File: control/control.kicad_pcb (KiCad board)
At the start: 2 copper layers, 39.1 x 45.8 mm, 37 parts, among them J1 AVR-ISP-6, J2 Conn_01x07_Pin, J3 Conn_01x02_Pin, J4 Conn_01x04_Socket, P1 Conn_01x03_Pin, P2 Conn_01x03_Pin, P3 Conn_01x03_Pin, P4 Conn_01x03_Pin, SW1 SW_Push, U2 ATmega328P-A, Y1 16MHz

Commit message: Revised hardware
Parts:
- removed HOLE1, HOLE2: MountingHole_3.2mm_M3, MountingHole:MountingHole_3.2mm_M3
- removed LED1: LED1, LED_THT:LED_D4.0mm
- removed SW1: SW_Push, Button_Switch_SMD:SW_SPST_SKQG_WithoutStem
- added C12: 0.1uF, Capacitor_SMD:C_0805_2012Metric, F.Cu at (135.7, 84.4)
- added C14: 22uF, Capacitor_SMD:C_0805_2012Metric, F.Cu at (141.7, 90.8)
- added C15: 22uF, Capacitor_SMD:C_0805_2012Metric, F.Cu at (143.8, 90.8)
- added C16: 22uF, Capacitor_SMD:C_0805_2012Metric, F.Cu at (145.9, 90.8)
- added C17: 0.1uF, Capacitor_SMD:C_0805_2012Metric, F.Cu at (150.1, 87.3)
- added I2C1: FS2, Connector_JST:JST_XH_B4B-XH-A_1x04_P2.50mm_Vertical, F.Cu at (126.4, 60.6)
- added I2C2: FS1, Connector_JST:JST_XH_B4B-XH-A_1x04_P2.50mm_Vertical, F.Cu at (161.1, 60.6)
- added ISC3: MAIN, Connector_JST:JST_XH_B5B-XH-A_1x05_P2.50mm_Vertical, F.Cu at (156.2, 98.1)
- added JP1: Jumper_3_Open, Jumper:SolderJumper-3_P2.0mm_Open_TrianglePad1.0x1.5mm, F.Cu at (151.7, 80.2)
- added L2: 3.3uH, Inductor_SMD:L_Taiyo-Yuden_NR-60xx, F.Cu at (130.6, 85.4)
- added LED9: LED1, LED_THT:LED_D4.0mm, F.Cu at (131.4, 74.1)
- added R6: 33.2k, Resistor_SMD:R_0603_1608Metric, F.Cu at (152.5, 91.0)
- added R7: 10k, Resistor_SMD:R_0603_1608Metric, F.Cu at (138.9, 87.8)
- added R8: 10k, Resistor_SMD:R_0603_1608Metric, F.Cu at (138.6, 90.9)
- added R9: 54.9k, Resistor_SMD:R_0603_1608Metric, F.Cu at (125.8, 91.8)
- added REF**: MountingHole_3.2mm_M3, MountingHole:MountingHole_3.2mm_M3, F.Cu at (119.3, 95.3)
- added REF**: MountingHole_3.2mm_M3, MountingHole:MountingHole_3.2mm_M3, F.Cu at (131.3, 67.8)
- added S5: Conn_01x03_Pin, Connector_JST:JST_EH_B3B-EH-A_1x03_P2.50mm_Vertical, F.Cu at (124.0, 88.5)
- added SW2: SW_Push, Button_Switch_SMD:SW_SPST_B3U-1000P-B, F.Cu at (152.1, 74.7)
- added U3: ~, Package_TO_SOT_SMD:TSOT-23-6, F.Cu at (146.9, 87.3)
- C1, C2, C3, C4: value 22uF -> 100n; footprint Capacitor_SMD:C_0805_2012Metric -> Capacitor_SMD:C_0603_1608Metric
- C10, C9: value 100nF -> 22uF
- C11: value 10nF -> 22uF
- C6, C7: value 0.1uF -> 22uF
- C8: value 1uF -> 22uF
- J1: value AVR-ISP-6 -> Conn_01x02_Pin; footprint Connector_PinHeader_2.54mm:PinHeader_2x03_P2.54mm_Vertical_SMD -> Connector_JST:JST_XH_B2B-XH-A_1x02_P2.50mm_Vertical
- J2: value Conn_01x07_Pin -> Conn_01x04_Male; footprint Connector_JST:JST_XH_B7B-XH-A_1x07_P2.50mm_Vertical -> Connector_PinHeader_2.54mm:PinHeader_1x04_P2.54mm_Horizontal
- J4: value Conn_01x04_Socket -> Conn_01x07_Pin; footprint Connector_JST:JST_XH_B4B-XH-A_1x04_P2.50mm_Vertical -> Connector_JST:JST_XH_B7B-XH-A_1x07_P2.50mm_Vertical
- R2: value 420 -> 10k
- R5: value 54.9k -> 420
- U1: value ~ -> STM32F103C8Tx; footprint Package_TO_SOT_SMD:TSOT-23-6 -> Package_QFP:LQFP-48_7x7mm_P0.5mm
- U2: value ATmega328P-A -> ~; footprint Package_QFP:TQFP-32_7x7mm_P0.8mm -> Package_TO_SOT_SMD:TSOT-23-6
- Y1: value 16MHz -> 8Mhz
- moved J4 45.3 mm to (147.5, 60.6), turned to 180 degrees
- moved J2 37.9 mm to (162.0, 87.2), turned to 0 degrees
- moved J3 37.6 mm to (125.9, 95.5), turned to 0 degrees
- moved P1 34.6 mm to (162.7, 66.8), turned to 180 degrees
- moved J1 31.2 mm to (147.8, 95.5), turned to 0 degrees
- moved S1 28.4 mm to (124.0, 66.3), turned to 180 degrees
- moved Y1 25.8 mm to (147.4, 73.2)
- moved S4 24.6 mm to (124.0, 82.8), turned to 180 degrees
- moved P4 23.0 mm to (162.7, 83.0), turned to 180 degrees
- moved P2 20.7 mm to (162.7, 72.0), turned to 180 degrees
- moved U1 20.0 mm to (140.9, 73.6), turned to 180 degrees
- moved R5 19.6 mm to (128.1, 80.2), turned to -90 degrees
- moved C3 17.9 mm to (133.1, 80.3)
- moved C5 17.9 mm to (141.7, 87.3)
- moved C4 17.5 mm to (134.7, 80.3), turned to -90 degrees
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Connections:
- C1 pad 2: +5V -> +3.3V
- C10 pad 1: +5V -> +BATT
- C11 pad 1: +5V -> +BATT
- C2 pad 2: +5V -> +3.3V
- C3 pad 1: +BATT -> GND
- C3 pad 2: GND -> +3.3V
- C4 pad 1: +BATT -> +3.3V
- C5 pad 1: +BATT -> GND
- C5 pad 2: GND -> +3.3V
- C6 pad 1: Net-(U1-SW) -> GND
- C6 pad 2: Net-(U1-VBST) -> +3.3V
- C7 pad 1: Net-(U1-VFB) -> GND
- C8 pad 1: +5V -> GND
- C8 pad 2: GND -> +5V
- C9 pad 1: +5V -> +BATT
- J1 pad 1: MISO -> GND
- J1 pad 2: +5V -> +3.3V
- J2 pad 1: +5V -> +3.3V
- J2 pad 2: LED_{FIELD1} -> SWCLK
- J2 pad 3: LED_{FIELD2} -> SWDIO
- J2 pad 4: LED_{FIELD3} -> GND
- J4 pad 1: GND -> +5V
- J4 pad 2: +5V -> LED_{FIELD1}
- J4 pad 3: SDA -> LED_{FIELD2}
- J4 pad 4: SCL -> LED_{FIELD3}
- L1 pad 1: +5V -> +3.3V
- L1 pad 2: Net-(U1-SW) -> Net-(U3-SW)
- P1 pad 1: +5V -> +3.3V
- P2 pad 1: +5V -> +3.3V
- P3 pad 1: +5V -> +3.3V
- P4 pad 1: +5V -> +3.3V
- R1 pad 1: RESET -> GND
- R1 pad 2: +5V -> Net-(JP1-C)
- R2 pad 1: Net-(LED1-A) -> +3.3V
- R2 pad 2: +5V -> Net-(U1-NRST)
- R3 pad 2: Net-(U1-VFB) -> Net-(U3-VFB)
- R4 pad 1: Net-(U1-EN) -> Net-(U3-EN)
- R5 pad 1: +5V -> Net-(LED9-A)
- R5 pad 2: Net-(U1-VFB) -> +5V
- U1 pad 1: GND -> unconnected-(U1-VBAT-Pad1)
- U1 pad 2: Net-(U1-SW) -> unconnected-(U1-PC13-Pad2)
- U1 pad 3: +BATT -> unconnected-(U1-PC14-Pad3)
- U1 pad 4: Net-(U1-VFB) -> unconnected-(U1-PC15-Pad4)
- U1 pad 5: Net-(U1-EN) -> Net-(U1-PD0)
- U1 pad 6: Net-(U1-VBST) -> Net-(U1-PD1)
- U2 pad 1: LED_{FIELD4} -> GND
- U2 pad 2: unconnected-(U2-PD4-Pad2) -> Net-(U2-SW)
- U2 pad 3: GND -> +BATT
- U2 pad 4: +5V -> Net-(U2-VFB)
- U2 pad 5: GND -> Net-(U2-EN)
- U2 pad 6: +5V -> Net-(U2-VBST)
- Y1 pad 1: Net-(U2-XTAL2/PB7) -> Net-(U1-PD0)
- Y1 pad 3: Net-(U2-XTAL1/PB6) -> Net-(U1-PD1)
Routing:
- net +3.3V: track 0.00 -> 135.6 mm, vias 0 -> 3
- net SCL_{TOCTRL}: track 0.00 -> 55.9 mm
- net SDA_{TOCTRL}: track 0.00 -> 43.3 mm, vias 0 -> 2
- net SDA_{TOMAIN}: track 0.00 -> 41.0 mm, vias 0 -> 1
- net +5V: track 82.1 -> 45.2 mm, vias 11 -> 8
- net SWDIO: track 0.00 -> 33.4 mm, vias 0 -> 1
- net SWCLK: track 0.00 -> 32.2 mm, vias 0 -> 1
- net SER5: track 0.00 -> 27.4 mm, vias 0 -> 2
- net RESET: track 26.8 -> 0.00 mm, vias 4 -> 0
- net SCL_{TOMAIN}: track 0.00 -> 23.7 mm, vias 0 -> 1
- net BUZ: track 34.1 -> 11.6 mm, vias 2 -> 0
- net SCK: track 21.2 -> 0.00 mm, vias 2 -> 0
- net SDA: track 20.4 -> 0.00 mm, vias 1 -> 0
- net SCL: track 20.3 -> 0.00 mm, vias 1 -> 0
- net MISO: track 19.8 -> 0.00 mm, vias 2 -> 0
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- added copper zone on F.Cu, net +3.3V
- added copper zone on F.Cu, net +BATT
- added copper zone on B.Cu, net GND
- removed copper zone on F.Cu, net +5V
- removed copper zone on B.Cu, net +BATT
- removed copper zone on F.Cu, net GND
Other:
- board size 39.1 x 45.8 mm -> 50.3 x 43.1 mm
- board text added: "+BATT"
- board text added: "3"
- board text added: "3.3V"
- board text added: "5V"
- board text added: "BUZ"
- board text added: "C"
- board text added: "D"
- board text added: "F1"
- board text added: "F2"
- board text added: "F3"
- board text added: "F4"
- board text added: "G"
- board text added: "SCL"
- board text added: "SDA"
- board text removed: "Abdullah Alsafar"
- board text removed: "Distance between the center of the 2 mounting holes is 18.4532mm X: 18.4000mm Y: 1.4000mm"
- board text removed: "Distance from top-left corner to bottom-right corner: 60.1820mm X: 39.1000mm Y: 45.7500mm"
- board text removed: "Falcon Control Board"
- board text removed: "Human Powered Vehicles (DESIGN TEAM)"

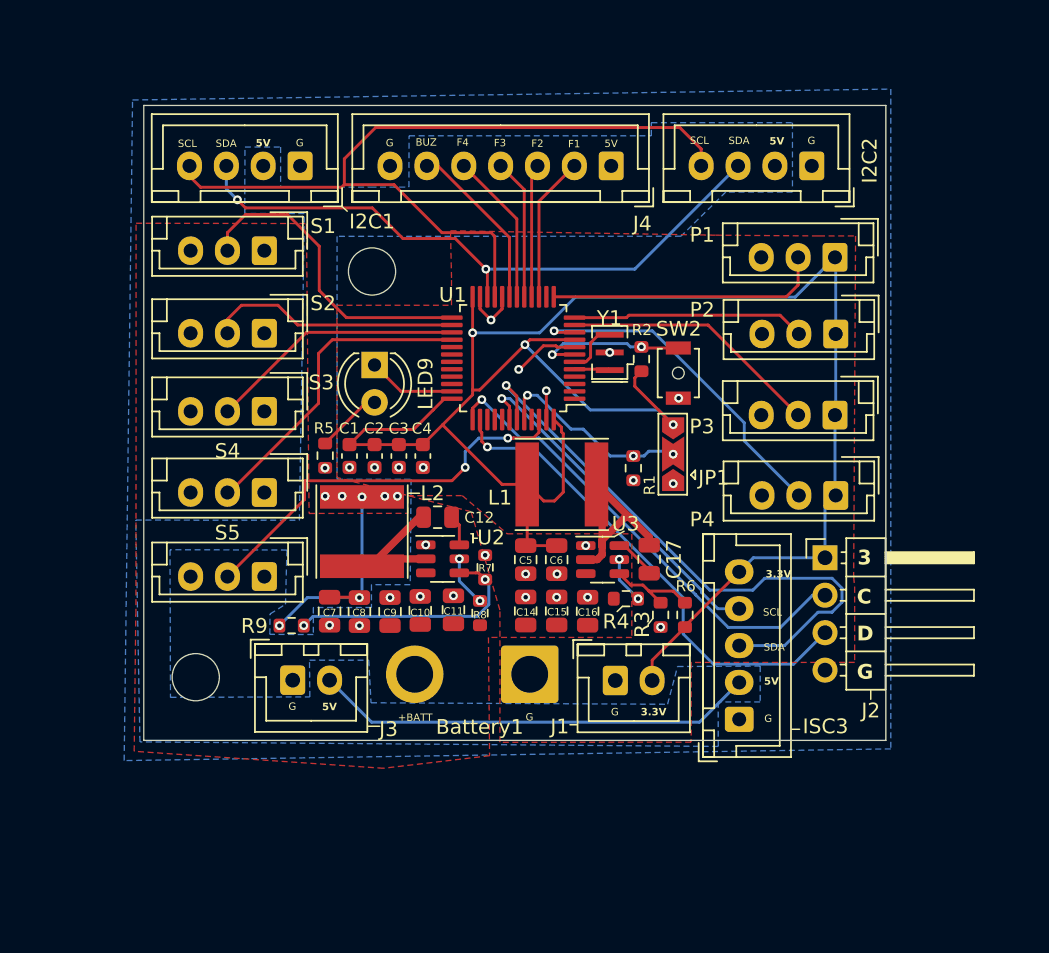
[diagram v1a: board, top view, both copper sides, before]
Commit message: Touch ups for control board
- Made adjustments to the placement of the decoupling capacitors for the STM32.
- Rotated some capacitors for VBATT pour
- Removed reference designators for most components
- Added some labels for the main power headers
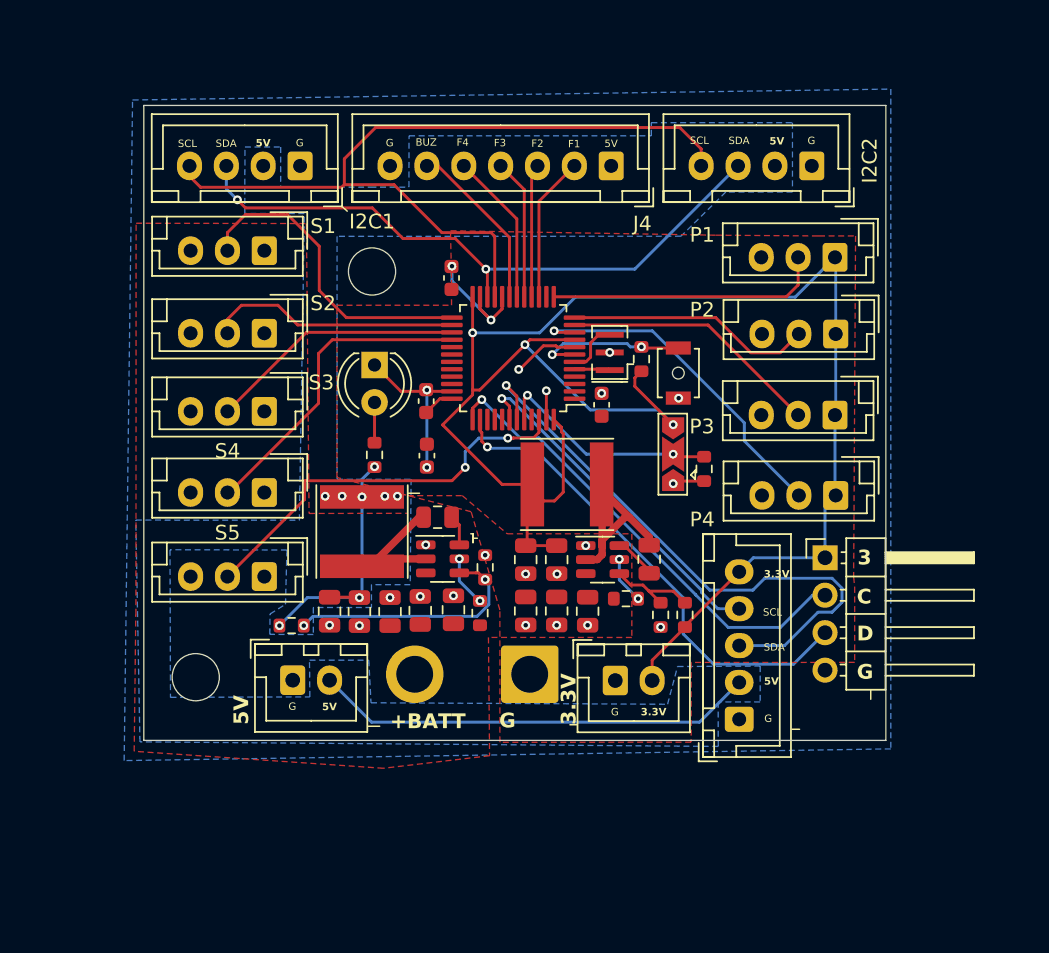
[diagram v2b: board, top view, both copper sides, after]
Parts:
- moved C1 13.9 mm to (136.7, 68.2), turned to -90 degrees
- moved C4 12.6 mm to (146.8, 76.8), turned to 90 degrees
- moved R1 4.80 mm to (153.8, 81.2)
- moved C3 4.16 mm to (134.9, 76.5), turned to -90 degrees
- moved C2 3.55 mm to (135.0, 80.2)
- moved R5 3.35 mm to (131.4, 80.2)
- moved L1 0.35 mm to (144.5, 82.2)
- turned C14 to -90 degrees
- turned C15 to -90 degrees
- turned C16 to -90 degrees
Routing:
- net GND: track 16.2 -> 28.4 mm, vias 25 -> 24
- net +3.3V: track 135.6 -> 123.6 mm
- net +5V: track 45.2 -> 47.6 mm
- net Net-(JP1-C): track 13.5 -> 15.4 mm, vias 3 -> 2
- net Net-(LED9-A): track 4.50 -> 2.73 mm
- net POT2: track 15.8 -> 16.7 mm

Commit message: added name, title, company, revision # & authors
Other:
- board text added: "Abdullah Alsafar Falcon Control Board"
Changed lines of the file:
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@@
   (paper "A4")
   (title_block
-    (title "Aircraft Joystick Reader & Regulator - Main Board")
-    (date "2023-06-03")
-    (rev "5")
+    (title "Falcon Control MAIN")
+    (date "2023-11-30")
+    (rev "15")
     (company "Human Powered Vehicles Design Team @ UOFT")
+    (comment 1 "Supervised by Savo Bajic")
+    (comment 2 "Designed by Abdullah Alsafar")
   )
   (layers
@@
     (effects (font (size 0.5 0.5) (thickness 0.1) bold) (justify left bottom))
   )
+  (gr_text "Abdullah Alsafar\nFalcon Control Board" (at 136 66.75) (layer "F.SilkS")
+    (effects (font (size 1 1) (thickness 0.15)) (justify left bottom))
+  )
   (gr_text "G" (at 126.11 59.33) (layer "F.SilkS")

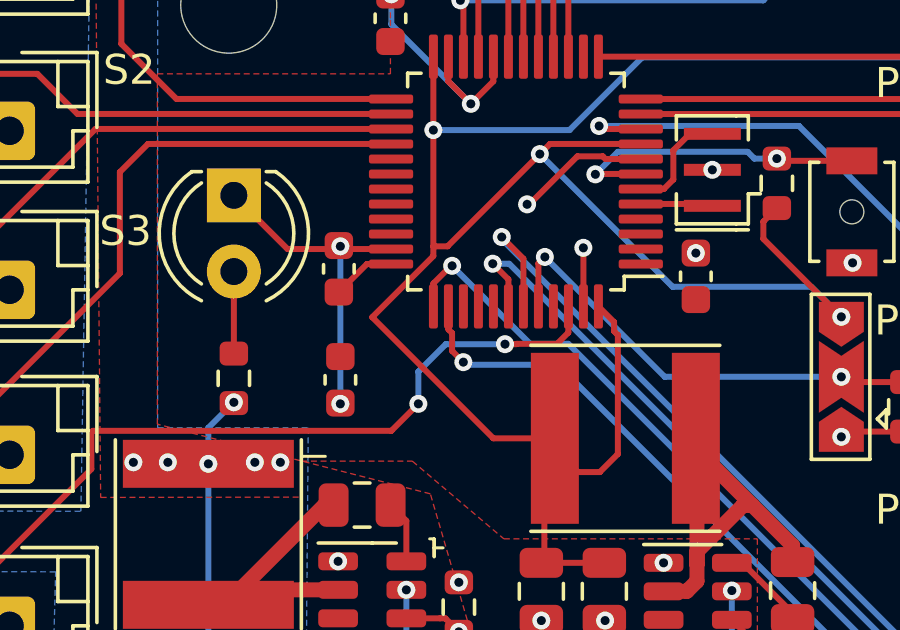
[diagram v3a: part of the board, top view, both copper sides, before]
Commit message: changed SWDIO pin from 38 to 34
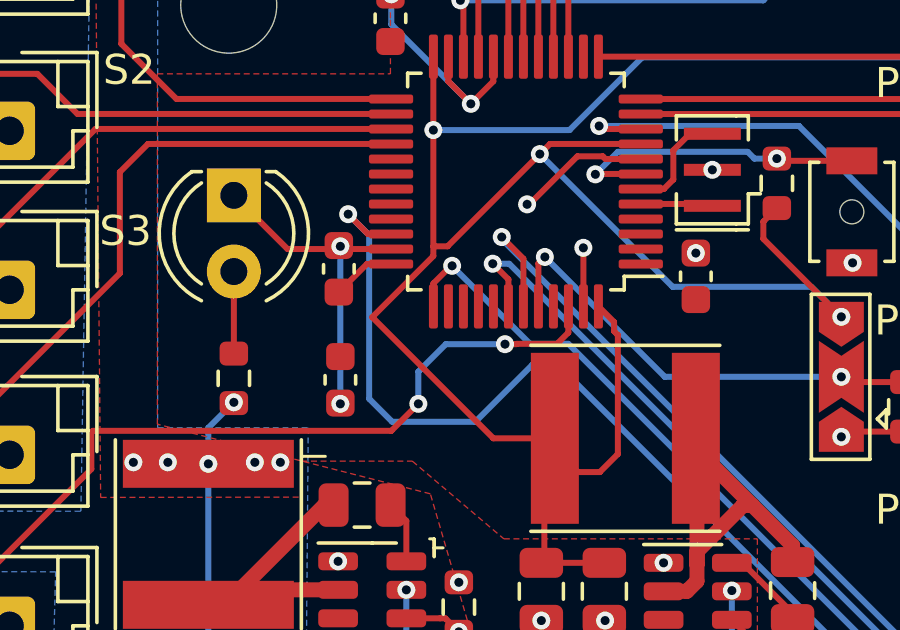
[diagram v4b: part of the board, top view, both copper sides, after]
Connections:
- U1 pad 34: unconnected-(U1-PA13-Pad34) -> SWDIO
- U1 pad 38: SWDIO -> unconnected-(U1-PA15-Pad38)
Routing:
- net SWDIO: track 33.4 -> 43.7 mm
